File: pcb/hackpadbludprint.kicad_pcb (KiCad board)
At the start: 2 copper layers, 32.6 x 98.7 mm, 6 parts, among them SW1 SW_Push, SW2 SW_Push, SW3 SW_Push, SW4 SW_Push, U1 MOUDLE-SEEEDUINO-XIAO

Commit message: STRETCH 3!!!!
- board looking nice
- Tysm jame
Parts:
- added D2: SK6812MINI-E, LED_SMD:LED_SK6812MINI-E_3.2x2.8mm_P1.5mm_ReverseMount, B.Cu at (150.5, 104.4)
- added D3: SK6812MINI-E, LED_SMD:LED_SK6812MINI-E_3.2x2.8mm_P1.5mm_ReverseMount, B.Cu at (150.5, 123.5)
- added D4: SK6812MINI-E, LED_SMD:LED_SK6812MINI-E_3.2x2.8mm_P1.5mm_ReverseMount, B.Cu at (150.5, 142.5)
- added SW5: RotaryEncoder_Switch, Rotary_Encoder:RotaryEncoder_Alps_EC11E-Switch_Vertical_H20mm, F.Cu at (165.5, 111.0)
- added U2: ER_OLEDM0.91_1x-I2C, Display:ER_OLEDM0.91_1x-I2C, F.Cu at (164.0, 57.5)
- moved D1 35.6 mm to (150.5, 85.5)
- moved U1 0.20 mm to (150.4, 60.6)
- renumbered D2 to D1
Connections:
- D1 pad 2: Net-(D2-DIN) -> Net-(D1-DIN)
- U1 pad 1: unconnected-(U1-PA02_A0_D0-Pad1) -> Net-(U1-PA02_A0_D0)
- U1 pad 14: unconnected-(U1-5V-Pad14) -> +5V
- U1 pad 2: unconnected-(U1-PA4_A1_D1-Pad2) -> Net-(U1-PA4_A1_D1)
- U1 pad 3: unconnected-(U1-PA10_A2_D2-Pad3) -> Net-(U1-PA10_A2_D2)
- U1 pad 5: Net-(D2-DIN) -> Net-(U1-PA8_A4_D4_SDA)
- U1 pad 6: unconnected-(U1-PA9_A5_D5_SCL-Pad6) -> Net-(U1-PA9_A5_D5_SCL)
- U1 pad 7: unconnected-(U1-PB08_A6_D6_TX-Pad7) -> Net-(D1-DIN)
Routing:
- net +5V: track 0.00 -> 127.8 mm
- net GND: track 121.2 -> 233.2 mm
- net Net-(U1-PA4_A1_D1): track 0.00 -> 103.5 mm
- net Net-(U1-PA02_A0_D0): track 0.00 -> 76.3 mm
- net Net-(U1-PA10_A2_D2): track 0.00 -> 75.8 mm
- net Net-(U1-PA8_A4_D4_SDA): track 0.00 -> 36.2 mm
- net Net-(U1-PA9_A5_D5_SCL): track 0.00 -> 34.4 mm
- net Net-(D1-DIN): track 0.00 -> 21.0 mm
- net Net-(D2-DOUT): track 0.00 -> 19.8 mm
- net Net-(D3-DOUT): track 0.00 -> 19.8 mm
- net Net-(D1-DOUT): track 0.00 -> 19.7 mm
- net unconnected-(U1-PA4_A1_D1-Pad2): track 1.59 -> 0.00 mm
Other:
- board size 32.6 x 98.7 mm -> 88.6 x 98 mm
- board text added: "HWBludPad V1"

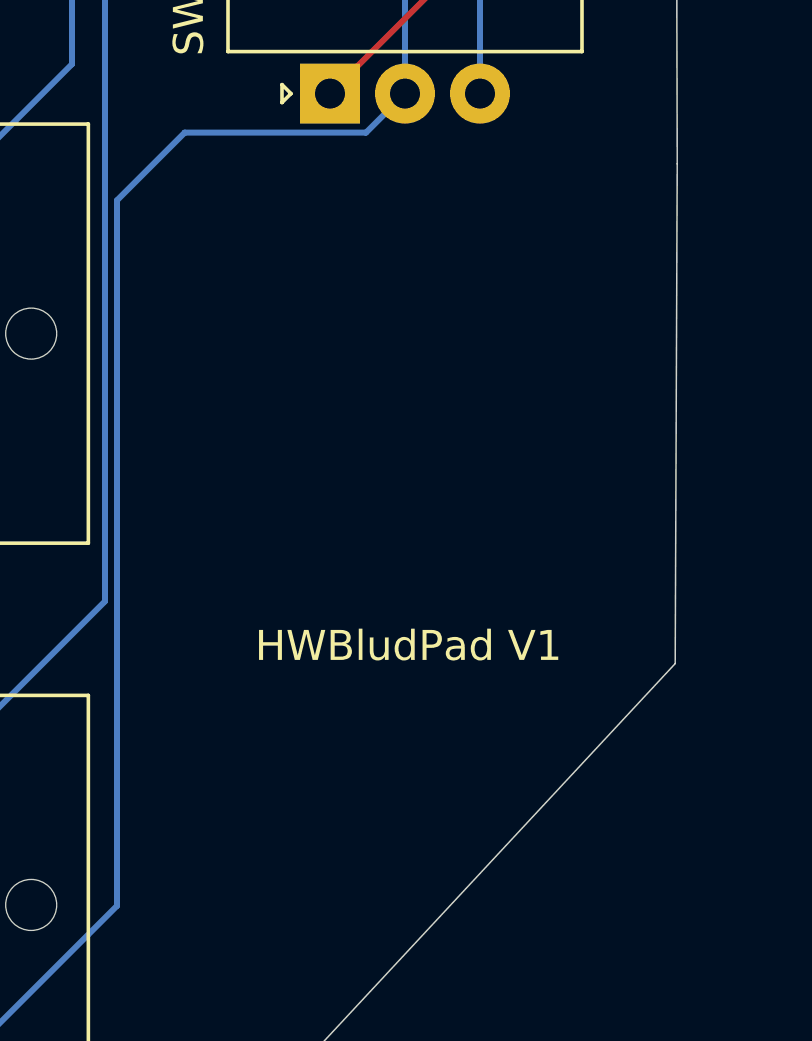
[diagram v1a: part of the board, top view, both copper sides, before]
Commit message: Deleted unused kicadproj
- Readme
- Added lawrence silksreen icon
- FIRMWARE moved here from home qmk folder in /users
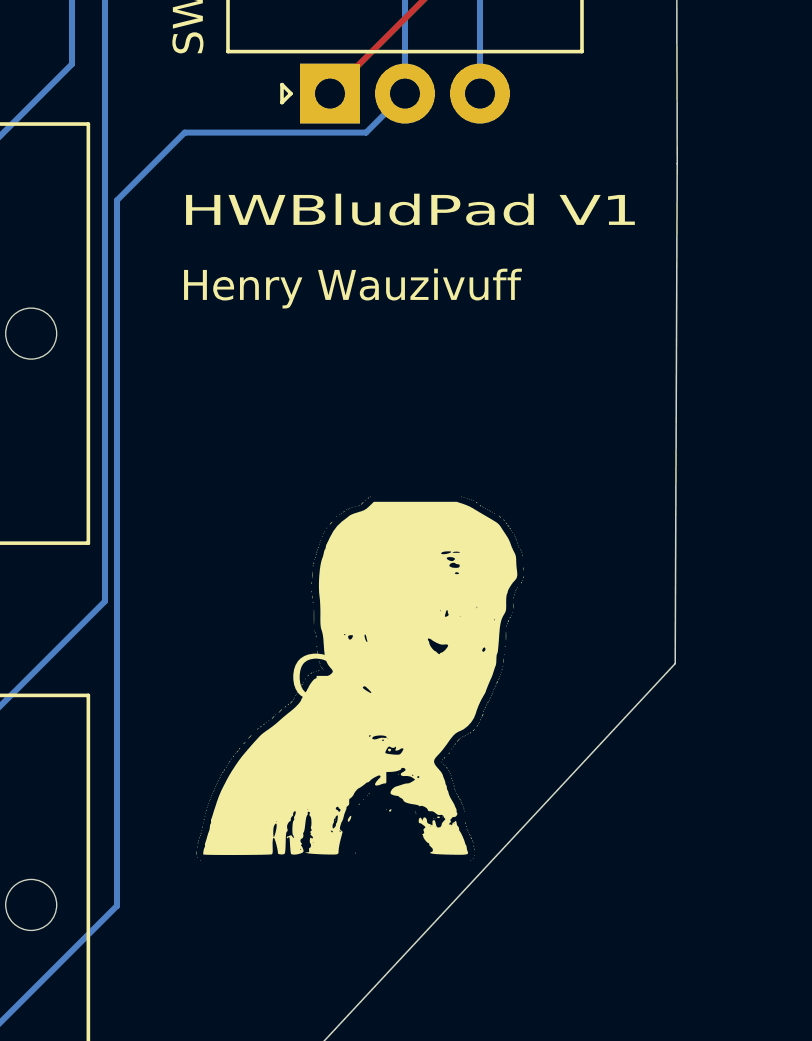
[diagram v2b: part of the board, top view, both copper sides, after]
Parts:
- added G***: LOGO, projftprints:lawrence_starin, F.Cu at (166.5, 130.5)
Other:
- board text added: "Henry Wauzivuff"

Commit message: FRIDGEE
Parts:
- moved G*** 4.50 mm to (166.5, 126.0)
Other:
- board size 88.6 x 98 mm -> 38.7 x 97.8 mm
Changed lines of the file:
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@@
 	(footprint "projftprints:lawrence_starin"
 		(layer "F.Cu")
-		(at 166.5 130.5)
+		(at 166.5 126)
 		(property "Reference" "G***"
 			(at 0 0 0)
@@
 	(gr_poly
 		(pts
-			(xy 176.919651 49.962542) (xy 138.423379 50.044625) (xy 138.631897 147.83824) (xy 160.466412 147.783309)
-			(xy 177.006951 130) (xy 177.074049 113.341597)
+			(xy 176.742818 49.95897) (xy 138.246536 50.041054) (xy 138.454986 147.802685) (xy 160.289501 147.747754)
+			(xy 176.83004 129.964445) (xy 176.897138 113.306042)
 		)
 		(stroke
@@
 		(layer "Edge.Cuts")
 	)
-	(gr_rect
-		(start 88.5 50)
-		(end 127.5 148)
-		(stroke
-			(width 0.05)
-			(type solid)
-		)
-		(fill no)
-		(layer "Edge.Cuts")
-	)
 	(gr_text "Henry Wauzivuff"
-		(at 160.5 118 0)
+		(at 160.5 117.5 0)
 		(layer "F.SilkS")
 		(effects
@@
 	)
 	(segment
-		(start 167.581533 50.581533)
-		(end 140.363117 50.636883)
+		(start 171.8 104.7)
+		(end 171.8 95.765685)
 		(width 0.2)
 		(layer "F.Cu")
@@
 	)
 	(segment
-		(start 173.57 56.57)
-		(end 167.581533 50.581533)
+		(start 140.359501 50.640499)
+		(end 139.546952 51.453048)
 		(width 0.2)
 		(layer "F.Cu")
@@
 	)
 	(segment
-		(start 165.5 111)
-		(end 171.8 104.7)
+		(start 167.582453 50.582453)
+		(end 140.359501 50.640499)
 		(width 0.2)
 		(layer "F.Cu")
@@
 	)
 	(segment
-		(start 173.57 93.995685)
-		(end 173.57 56.57)
+		(start 173.57 56.57)
+		(end 167.582453 50.582453)
 		(width 0.2)
 		(layer "F.Cu")
@@
 	)
 	(segment
-		(start 140.363117 50.636883)
-		(end 139.546952 51.453048)
+		(start 165.5 111)
+		(end 171.8 104.7)
 		(width 0.2)
 		(layer "F.Cu")
@@
 	)
 	(segment
-		(start 171.8 95.765685)
-		(end 173.57 93.995685)
+		(start 139.595293 55.54)
+		(end 142.75 55.54)
 		(width 0.2)
 		(layer "F.Cu")
@@
 	)
 	(segment
-		(start 139.595293 55.54)
-		(end 142.75 55.54)
+		(start 139.555181 55.499888)
+		(end 139.595293 55.54)
 		(width 0.2)
 		(layer "F.Cu")
@@
 	)
 	(segment
-		(start 171.8 104.7)
-		(end 171.8 95.765685)
+		(start 142.59 55.5)
+		(end 141 55.5)
 		(width 0.2)
 		(layer "F.Cu")
@@
 	)
 	(segment
-		(start 142.59 55.5)
-		(end 141 55.5)
+		(start 173.57 93.995685)
+		(end 173.57 56.57)
 		(width 0.2)
 		(layer "F.Cu")
@@
 	)
 	(segment
-		(start 139.555181 55.499888)
-		(end 139.595293 55.54)
+		(start 171.8 95.765685)
+		(end 173.57 93.995685)
 		(width 0.2)
 		(layer "F.Cu")
